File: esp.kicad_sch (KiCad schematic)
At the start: 22 parts, among them J11 USB_C_Receptacle_USB2.0_16P, SW2 SW_Nidec_CAS-120A1, U7 ESP-WROOM-02, U9 CH340K

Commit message: bit artık
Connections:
- net 3V3: no longer C63.2, C64.2, C65.1, R65.1, R66.1, R67.1, U7.1 (VDD), U9.10 (V3), U9.7 (VCC)
- new net +3V3: C63.2, C64.2, C65.1, R65.1, R66.1, R67.1, U7.1 (VDD), U9.10 (V3), U9.7 (VCC)

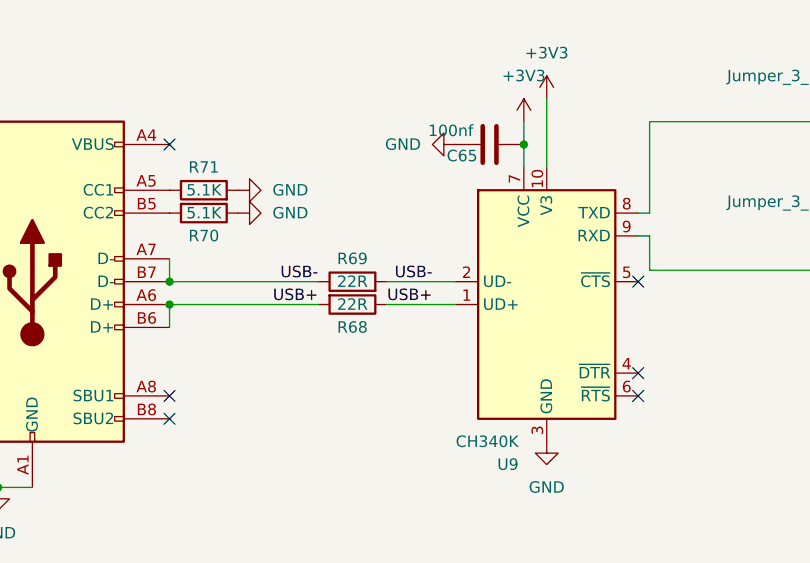
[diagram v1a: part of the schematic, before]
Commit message: esp-32 layout changes
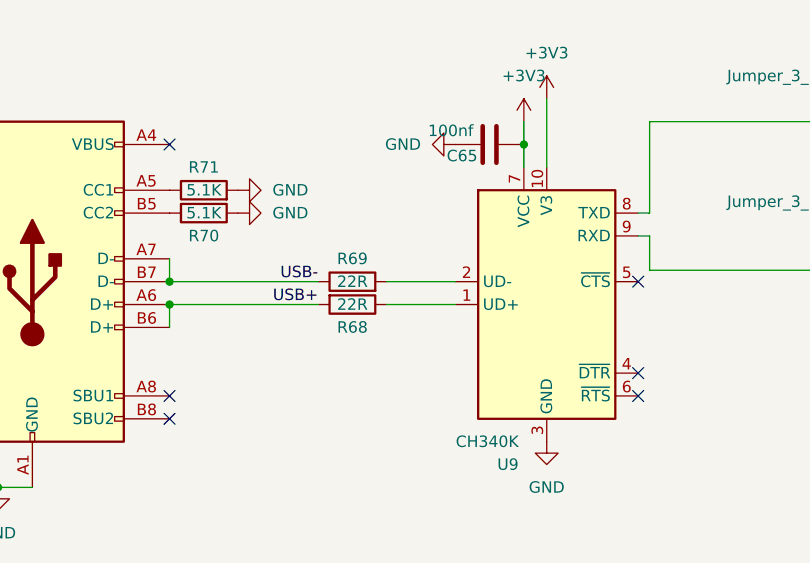
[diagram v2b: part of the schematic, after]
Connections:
- net USB+: no longer R68.1, U9.1 (UD+)
- net USB-: no longer R69.2, U9.2 (UD-)
- new net: R68.1, U9.1 (UD+)
- new net: R69.2, U9.2 (UD-)
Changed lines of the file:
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@@
-	)
-	(label "USB+"
-		(at 102.87 114.3 180)
-		(effects
-			(font
-				(size 1.27 1.27)
-			)
-			(justify right bottom)
-		)
-	)
-	(label "USB-"
-		(at 102.87 111.76 180)
-		(effects
-			(font
-				(size 1.27 1.27)
-			)
-			(justify right bottom)
-		)
 	)
 	(label "USB+"

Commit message: BMS DONE IHOPE
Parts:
- JP2, JP3: footprint Jumper:SolderJumper-3_P2.0mm_Open_TrianglePad1.0x1.5mm_NumberLabels -> Jumper:SolderJumper-3_P1.3mm_Bridged2Bar12_Pad1.0x1.5mm
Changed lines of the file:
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@@
+	(wire
+		(pts
+			(xy 156.21 95.25) (xy 163.83 95.25)
+		)
+		(stroke
+			(width 0)
+			(type default)
+		)
+	)
 	(wire
 		(pts
@@
 		(pts
 			(xy 73.66 111.76) (xy 73.66 109.22)
-		)
-		(stroke
-			(width 0)
-			(type default)
-		)
-	)
-	(wire
-		(pts
-			(xy 156.21 95.25) (xy 161.29 95.25)
 		)
 		(stroke
@@
 	(hierarchical_label "ESP_TX"
 		(shape output)
-		(at 161.29 95.25 0)
+		(at 163.83 95.25 0)
 		(effects
 			(font
@@
 			)
 		)
-		(property "Footprint" "Jumper:SolderJumper-3_P2.0mm_Open_TrianglePad1.0x1.5mm_NumberLabels"
+		(property "Footprint" "Jumper:SolderJumper-3_P1.3mm_Bridged2Bar12_Pad1.0x1.5mm"
 			(at 156.21 101.6 0)
 			(effects
@@
 			)
 		)
-		(property "Footprint" "Jumper:SolderJumper-3_P2.0mm_Open_TrianglePad1.0x1.5mm_NumberLabels"
+		(property "Footprint" "Jumper:SolderJumper-3_P1.3mm_Bridged2Bar12_Pad1.0x1.5mm"
 			(at 156.21 87.63 0)
 			(effects
